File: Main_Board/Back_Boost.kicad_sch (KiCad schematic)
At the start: 10 parts, among them U4 TPS63031DSK

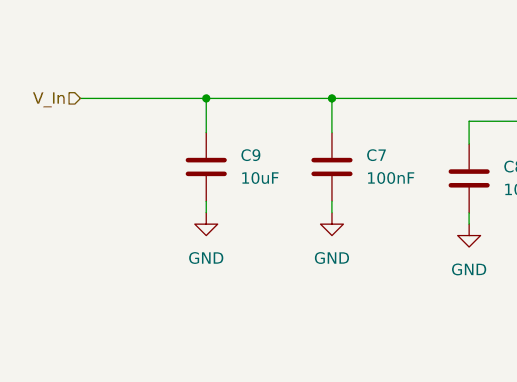
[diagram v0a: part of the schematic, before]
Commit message: Input Protection
Irlm is left to be calculated
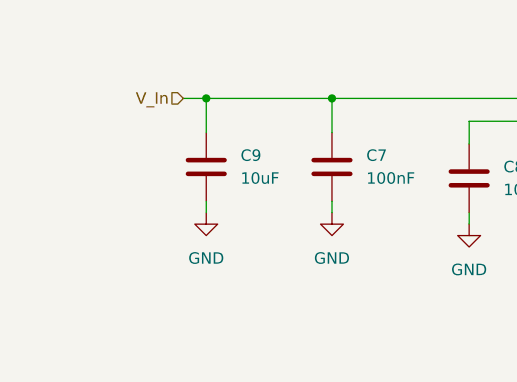
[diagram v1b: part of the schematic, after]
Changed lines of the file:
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@@
 	(paper "A4")
 	(junction
+		(at 67.31 63.5)
+		(diameter 0)
+		(color 0 0 0 0)
+	)
+	(junction
 		(at 187.96 63.5)
 		(diameter 0)
@@
 		(color 0 0 0 0)
 	)
-	(junction
-		(at 67.31 63.5)
-		(diameter 0)
-		(color 0 0 0 0)
-	)
 	(wire
 		(pts
@@
 	(wire
 		(pts
-			(xy 53.34 63.5) (xy 67.31 63.5)
+			(xy 64.77 63.5) (xy 67.31 63.5)
 		)
 		(stroke
@@
 			(width 0)
 			(type default)
+		)
+	)
+	(hierarchical_label "V_In"
+		(shape input)
+		(at 64.77 63.5 180)
+		(effects
+			(font
+				(size 1.27 1.27)
+			)
+			(justify right)
 		)
 	)
@@
 		(effects
 			(font
-				(size 1.27 1.27)
-			)
-			(justify right)
-		)
-	)
-	(hierarchical_label "V_In"
-		(shape input)
-		(at 53.34 63.5 180)
-		(effects
-			(font

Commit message: Aesthetics/cleanup
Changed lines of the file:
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@@
 	(paper "A4")
 	(junction
+		(at 187.96 63.5)
+		(diameter 0)
+		(color 0 0 0 0)
+	)
+	(junction
+		(at 162.56 63.5)
+		(diameter 0)
+		(color 0 0 0 0)
+	)
+	(junction
 		(at 67.31 63.5)
 		(diameter 0)
@@
 	)
 	(junction
-		(at 187.96 63.5)
-		(diameter 0)
-		(color 0 0 0 0)
-	)
-	(junction
-		(at 162.56 63.5)
-		(diameter 0)
-		(color 0 0 0 0)
-	)
-	(junction
 		(at 81.28 63.5)
 		(diameter 0)
@@
 	(wire
 		(pts
-			(xy 64.77 63.5) (xy 67.31 63.5)
+			(xy 62.23 63.5) (xy 67.31 63.5)
 		)
 		(stroke
@@
 	(hierarchical_label "V_In"
 		(shape input)
-		(at 64.77 63.5 180)
+		(at 62.23 63.5 180)
 		(effects
 			(font

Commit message: Add buzzer, Add LED, ADD R&D jumper
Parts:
- renumbered C8 to C10, C10 to C12, C12 to C13, C9 to C8, C7 to C9, D3 to D4, L2 to L1, R7 to R23, U4 to U3

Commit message: ADD footprints
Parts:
- C10, C11, C12, C13, C8, C9: footprint (none) -> Capacitor_SMD:C_0603_1608Metric
- D4: footprint (none) -> Diode_SMD:D_0603_1608Metric
- L1: footprint (none) -> Inductor_SMD:L_Taiyo-Yuden_MD-3030; PN (none) -> LQH3NPN1R5MJRL
- R23: footprint (none) -> Resistor_SMD:R_0603_1608Metric
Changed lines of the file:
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@@
 			)
 		)
-		(property "Footprint" ""
+		(property "Footprint" "Inductor_SMD:L_Taiyo-Yuden_MD-3030"
 			(at 115.57 78.74 0)
 			(hide yes)
@@
 			)
 		)
-		(property "Datasheet" ""
+		(property "Datasheet" "LQH3NPN1R5MJRL"
 			(at 115.57 78.74 0)
 			(hide yes)
@@
 		)
 		(property "Description" "Inductor, small symbol"
+			(at 115.57 78.74 0)
+			(hide yes)
+			(show_name no)
+			(do_not_autoplace no)
+			(effects
+				(font
+					(size 1.27 1.27)
+				)
+			)
+		)
+		(property "PN" "LQH3NPN1R5MJRL"
 			(at 115.57 78.74 0)
 			(hide yes)
@@
 			)
 		)
-		(property "Footprint" ""
+		(property "Footprint" "Capacitor_SMD:C_0603_1608Metric"
 			(at 176.2252 74.93 0)
 			(hide yes)
@@
 			)
 		)
-		(property "Footprint" ""
+		(property "Footprint" "Capacitor_SMD:C_0603_1608Metric"
 			(at 147.0152 74.93 0)
 			(hide yes)
@@
 			)
 		)
-		(property "Footprint" ""
+		(property "Footprint" "Diode_SMD:D_0603_1608Metric"
 			(at 187.96 67.31 0)
 			(hide yes)
@@
 			)
 		)
-		(property "Footprint" ""
+		(property "Footprint" "Capacitor_SMD:C_0603_1608Metric"
 			(at 163.5252 74.93 0)
 			(hide yes)
@@
 			)
 		)
-		(property "Footprint" ""
+		(property "Footprint" "Capacitor_SMD:C_0603_1608Metric"
 			(at 82.2452 74.93 0)
 			(hide yes)
@@
 			)
 		)
-		(property "Footprint" ""
+		(property "Footprint" "Resistor_SMD:R_0603_1608Metric"
 			(at 186.182 76.2 90)
 			(hide yes)
@@
 			)
 		)
-		(property "Footprint" ""
+		(property "Footprint" "Capacitor_SMD:C_0603_1608Metric"
 			(at 68.2752 74.93 0)
 			(hide yes)
@@
 			)
 		)
-		(property "Footprint" ""
+		(property "Footprint" "Capacitor_SMD:C_0603_1608Metric"
 			(at 97.4852 76.2 0)
 			(hide yes)

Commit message: PCB init
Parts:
- removed D4: LED, Diode_SMD:D_0603_1608Metric, symbol Device:LED
- removed R23: 330R, Resistor_SMD:R_0603_1608Metric, symbol Device:R

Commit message: Fix schematic readibility
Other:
- moved on the sheet: C10, C11, C12, C13, C8, C9, L1, U3
